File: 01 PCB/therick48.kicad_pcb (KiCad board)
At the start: 2 copper layers, 226.5 x 75.8 mm, 133 parts, among them J1 TYPE-C-31-M12_13, J2 AVR-ISP-6_mod, K1 KEYSW, K10 KEYSW, K11 KEYSW, K12 KEYSW, K13 KEYSW, K14 KEYSW, K15 KEYSW, K16 KEYSW, K17 KEYSW, K18 KEYSW, K19 KEYSW, K2 KEYSW, K20 KEYSW, K21 KEYSW, K22 KEYSW, K23 KEYSW, K24 KEYSW, K25 KEYSW, K26 KEYSW, K27 KEYSW, K28 KEYSW, K29 KEYSW, K3 KEYSW, K30 KEYSW, K31 KEYSW, K32 KEYSW, K33 KEYSW, K34 KEYSW, K35 KEYSW, K36 KEYSW, K37 KEYSW, K38 KEYSW, K39 KEYSW, K4 KEYSW, K40 KEYSW, K41 KEYSW, K42 KEYSW, K43 KEYSW, K44 KEYSW, K45 KEYSW, K46 KEYSW, K47 KEYSW, K48 KEYSW, K5 KEYSW, K6 KEYSW, K7 KEYSW, K8 KEYSW, K9 KEYSW, SW1 SW_PUSH, U1 ATMEGA32U4, U2 HOLE, U3 USBLC6-2SC6, U4 HOLE, Y1 16MHz

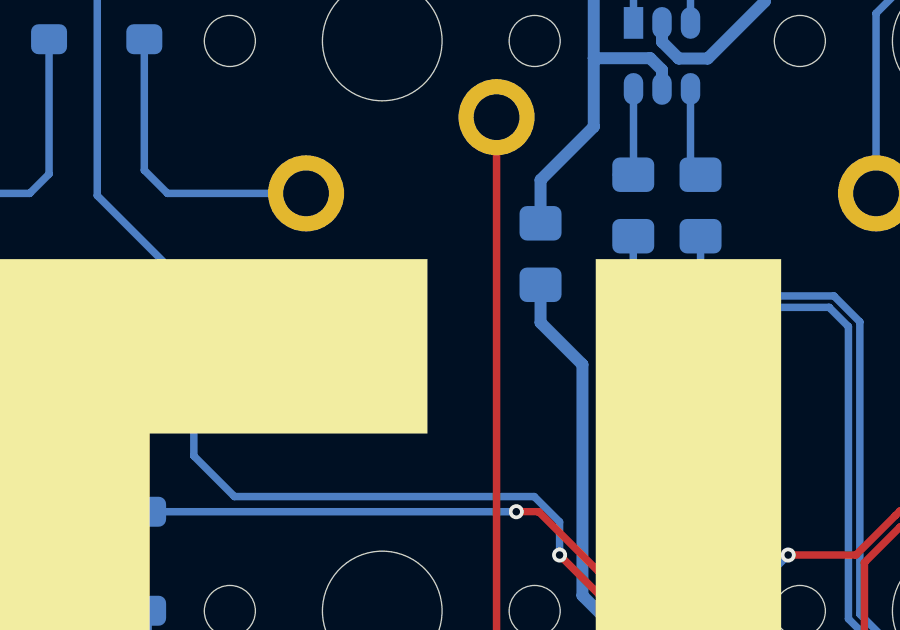
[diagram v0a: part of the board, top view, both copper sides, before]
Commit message: Add power LED
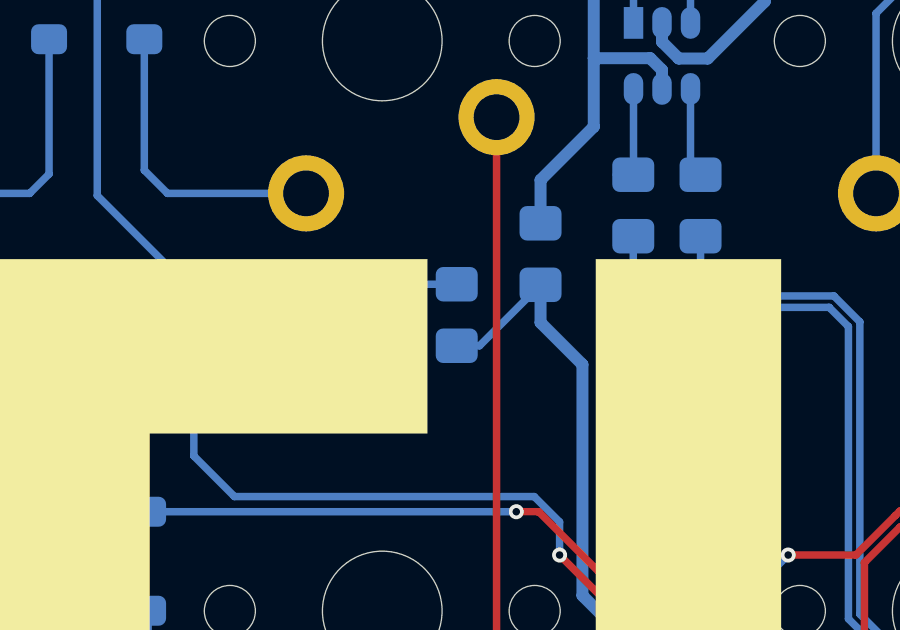
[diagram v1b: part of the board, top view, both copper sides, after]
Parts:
- added LED1: LED, LED_SMD:LED_0805_2012Metric_Pad1.15x1.40mm_HandSolder, B.Cu at (74.3, 53.6)
- added R4: 1K, Resistor_SMD:R_0805_2012Metric_Pad1.15x1.40mm_HandSolder, B.Cu at (77.0, 53.6)
- added U5: HOLE, Symbol:OSHW-Logo2_9.8x8mm_SilkScreen, B.Cu at (55.9, 93.3)
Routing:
- net VCC: track 228.8 -> 232.4 mm
- net Net-(LED1-Pad2): track 0.00 -> 2.67 mm

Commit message: Add power LED
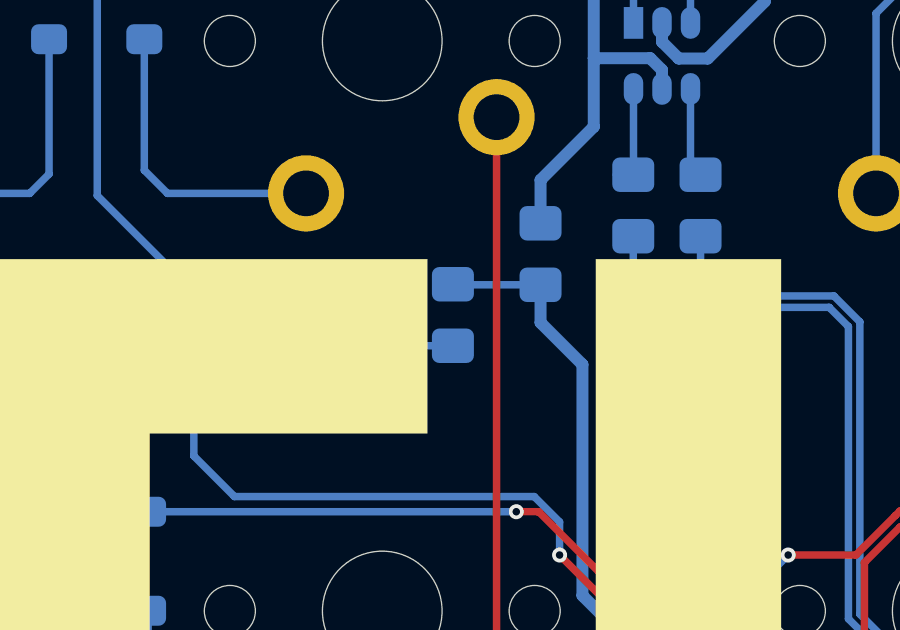
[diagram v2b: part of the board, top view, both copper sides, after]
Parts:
- moved R4 0.13 mm to (76.8, 53.6), turned to 90 degrees
- turned LED1 to 270 degrees
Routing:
- net VCC: track 232.4 -> 231.7 mm
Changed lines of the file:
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@@
     (add_net "Net-(D9-Pad2)")
     (add_net "Net-(J1-PadA5)")
-    (add_net "Net-(J1-PadA8)")
     (add_net "Net-(J1-PadB5)")
-    (add_net "Net-(J1-PadB8)")
     (add_net "Net-(LED1-Pad2)")
     (add_net "Net-(R1-Pad2)")
     (add_net "Net-(R2-Pad1)")
     (add_net "Net-(R3-Pad1)")
-    (add_net "Net-(U1-Pad18)")
-    (add_net "Net-(U1-Pad19)")
-    (add_net "Net-(U1-Pad20)")
-    (add_net "Net-(U1-Pad21)")
-    (add_net "Net-(U1-Pad28)")
-    (add_net "Net-(U1-Pad29)")
-    (add_net "Net-(U1-Pad30)")
-    (add_net "Net-(U1-Pad31)")
-    (add_net "Net-(U1-Pad32)")
-    (add_net "Net-(U1-Pad42)")
     (add_net VBUS)
     (add_net VCC)
@@
   )
   (module LED_SMD:LED_0805_2012Metric_Pad1.15x1.40mm_HandSolder (layer B.Cu)
-    (at 74.295 53.594 90)
+    (at 74.295 53.594 270)
     (descr "LED SMD 0805 (2012 Metric), square (rectangular) end terminal, IPC_7351 nominal, (Body size source: https://docs.google.com/spreadsheets/d/1BsfQQcO9C6DZCsRaXUlFlo91Tg2WpOkGARC1WS5S8t0/edit?usp=sharing), generated with kicad-footprint-generator")
     (tags "LED handsolder")
     (attr smd)
-    (fp_text reference LED1 (at -3.302 0 90) (layer B.SilkS)
+    (fp_text reference LED1 (at 3.302 0 90) (layer B.SilkS)
       (effects (font (size 0.8 0.7) (thickness 0.15)) (justify mirror))
     )
@@
     (fp_line (start -0.7 0.6) (end -1 0.3) (layer B.Fab) (width 0.1))
     (fp_line (start 1 0.6) (end -0.7 0.6) (layer B.Fab) (width 0.1))
-    (pad 2 smd roundrect (at 1.025 0 90) (size 1.15 1.4) (layers B.Cu B.Paste B.Mask) (roundrect_rratio 0.217391)
+    (pad 2 smd roundrect (at 1.025 0 270) (size 1.15 1.4) (layers B.Cu B.Paste B.Mask) (roundrect_rratio 0.217391)
       (net 81 "Net-(LED1-Pad2)"))
-    (pad 1 smd roundrect (at -1.025 0 90) (size 1.15 1.4) (layers B.Cu B.Paste B.Mask) (roundrect_rratio 0.217391)
+    (pad 1 smd roundrect (at -1.025 0 270) (size 1.15 1.4) (layers B.Cu B.Paste B.Mask) (roundrect_rratio 0.217391)
       (net 80 GND))
     (model ${KISYS3DMOD}/LED_SMD.3dshapes/LED_0805_2012Metric.wrl
@@
   )
   (module Resistor_SMD:R_0805_2012Metric_Pad1.15x1.40mm_HandSolder (layer B.Cu)
-    (at 76.962 53.594 270)
+    (at 76.835 53.594 90)
     (descr "Resistor SMD 0805 (2012 Metric), square (rectangular) end terminal, IPC_7351 nominal with elongated pad for handsoldering. (Body size source: https://docs.google.com/spreadsheets/d/1BsfQQcO9C6DZCsRaXUlFlo91Tg2WpOkGARC1WS5S8t0/edit?usp=sharing), generated with kicad-footprint-generator")
     (tags "resistor handsolder")
     (attr smd)
-    (fp_text reference R4 (at 2.667 0 90) (layer B.SilkS)
+    (fp_text reference R4 (at -2.667 0 90) (layer B.SilkS)
       (effects (font (size 0.8 0.7) (thickness 0.15)) (justify mirror))
     )
@@
       (effects (font (size 1 1) (thickness 0.15)) (justify mirror))
     )
-    (fp_text user %V (at -2.54 0 180) (layer B.SilkS)
+    (fp_text user %V (at 2.54 0 180) (layer B.SilkS)
       (effects (font (size 0.8 0.7) (thickness 0.15)) (justify mirror))
     )
@@
     (fp_line (start -1 0.6) (end 1 0.6) (layer B.Fab) (width 0.1))
     (fp_line (start -1 -0.6) (end -1 0.6) (layer B.Fab) (width 0.1))
-    (pad 2 smd roundrect (at 1.025 0 270) (size 1.15 1.4) (layers B.Cu B.Paste B.Mask) (roundrect_rratio 0.217391)
+    (pad 2 smd roundrect (at 1.025 0 90) (size 1.15 1.4) (layers B.Cu B.Paste B.Mask) (roundrect_rratio 0.217391)
       (net 49 VCC))
-    (pad 1 smd roundrect (at -1.025 0 270) (size 1.15 1.4) (layers B.Cu B.Paste B.Mask) (roundrect_rratio 0.217391)
+    (pad 1 smd roundrect (at -1.025 0 90) (size 1.15 1.4) (layers B.Cu B.Paste B.Mask) (roundrect_rratio 0.217391)
       (net 81 "Net-(LED1-Pad2)"))
     (model ${KISYS3DMOD}/Resistor_SMD.3dshapes/R_0805_2012Metric.wrl
@@
   (segment (start 107.188 47.39375) (end 103.845852 47.39375) (width 0.25) (layer B.Cu) (net 49))
   (segment (start 105.537 58.674) (end 106.68 58.674) (width 0.25) (layer B.Cu) (net 49))
-  (segment (start 77.724 54.619) (end 76.962 54.619) (width 0.25) (layer B.Cu) (net 49))
-  (segment (start 79.756 52.587) (end 77.724 54.619) (width 0.25) (layer B.Cu) (net 49))
+  (segment (start 76.853 52.587) (end 76.835 52.569) (width 0.25) (layer B.Cu) (net 49))
+  (segment (start 79.756 52.587) (end 76.853 52.587) (width 0.25) (layer B.Cu) (net 49))
   (segment (start 85.725 52.959) (end 89.535 52.959) (width 0.25) (layer B.Cu) (net 50))
   (segment (start 85.09 50.968) (end 85.09 52.324) (width 0.25) (layer B.Cu) (net 50))
@@
   (segment (start 84.362 45.045) (end 83.805 44.488) (width 0.4) (layer B.Cu) (net 80))
   (segment (start 87.23 43.144) (end 85.329 45.045) (width 0.4) (layer B.Cu) (net 80))
-  (segment (start 76.962 52.569) (end 74.295 52.569) (width 0.25) (layer B.Cu) (net 81))
+  (segment (start 76.835 54.619) (end 74.295 54.619) (width 0.25) (layer B.Cu) (net 81))
   (zone (net 80) (net_name GND) (layer B.Cu) (hatch edge 0.508)
     (connect_pads (clearance 0.25))

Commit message: Gerber
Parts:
- U5: footprint Symbol:OSHW-Logo2_9.8x8mm_SilkScreen -> Symbol:OSHW-Logo_11.4x12mm_SilkScreen
- moved U5 104.2 mm to (160.0, 91.2)
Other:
- board text added: "github.com/dierickdie"
- board text added: "therick48 Rev 1.1"
- board text removed: "PCB Rev 1.1"
- board text removed: "therick48"
